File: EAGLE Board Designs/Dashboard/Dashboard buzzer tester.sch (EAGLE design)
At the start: 0 parts

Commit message: Buzzer test circuit additions
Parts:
- added C21: CAPACITOR_0603_10V_0.1UF, HyTechDevices:CAPACITOR_0603_10V_0.1UF
- added K1: CPC1002N, HyTechDevices - Copy:CPC1002N
- added Q7: TRANSISTOR_P_MOS_SOT23_SI2369DS-T1-GE3, HyTechDevices:TRANSISTOR_P_MOS_SOT23_SI2369DS-T1-GE3
- added R16: RESISTOR_0603_150K, HyTechDevices:RESISTOR_0603_150K
- added R17: RESISTOR_0603_2K, HyTechDevices:RESISTOR_0603_2K
- added R18: RESISTOR_0603_1K, HyTechDevices:RESISTOR_0603_1K
- added R19: RESISTOR_0603_620, HyTechDevices:RESISTOR_0603_620
- added R22: RESISTOR_0603_3.9K, HyTechDevices:RESISTOR_0603_3.9K
- added U$1: BUZZER_3_PIN_CPT-3011C-120, HyTechDevices:BUZZER_3_PIN_CPT-3011C-120
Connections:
- new net +12V: K1.DC+
- new net BUZZER_CTRL: K1.CONTROL+
- new net BUZZER_OUT: C21.1, K1.DC-, R17.1
- new net GND: C21.2, Q7.S, R17.2, R18.1, U$1.GND
- new net N$20: R16.2, R22.1, U$1.F
- new net N$22: Q7.G, R22.2
- new net N$29: R16.1, R19.1
- new net N$41: Q7.D, R19.2, U$1.VDD
- new net N$68: K1.CONTROL-, R18.2
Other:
- note added: "PCB for testing piezo buzzer for dashboard"
- note added: "Youssef Jaafar"

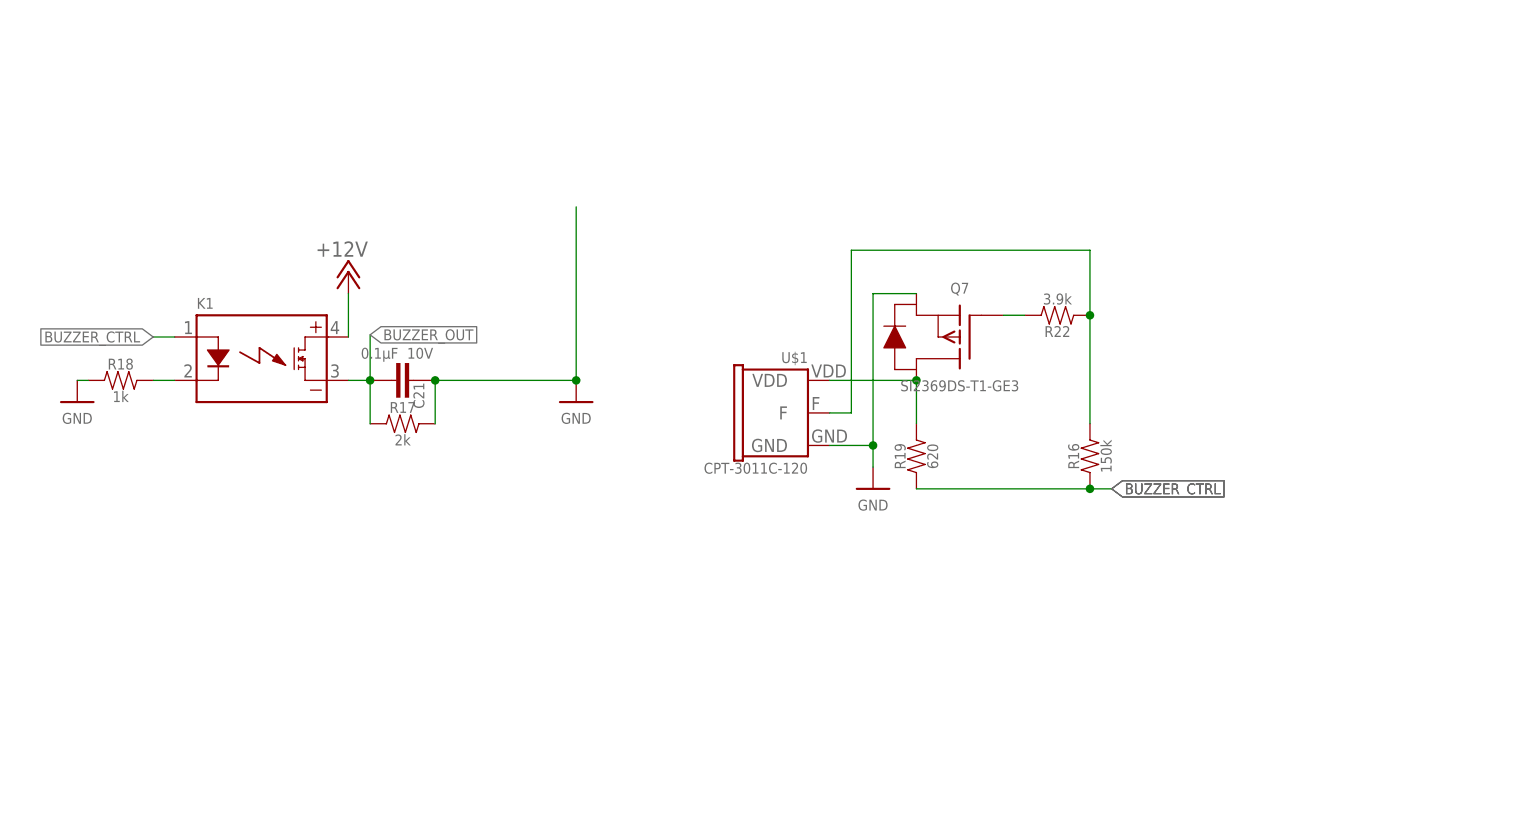
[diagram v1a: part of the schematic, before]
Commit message: Buzzer tester schematic and board started
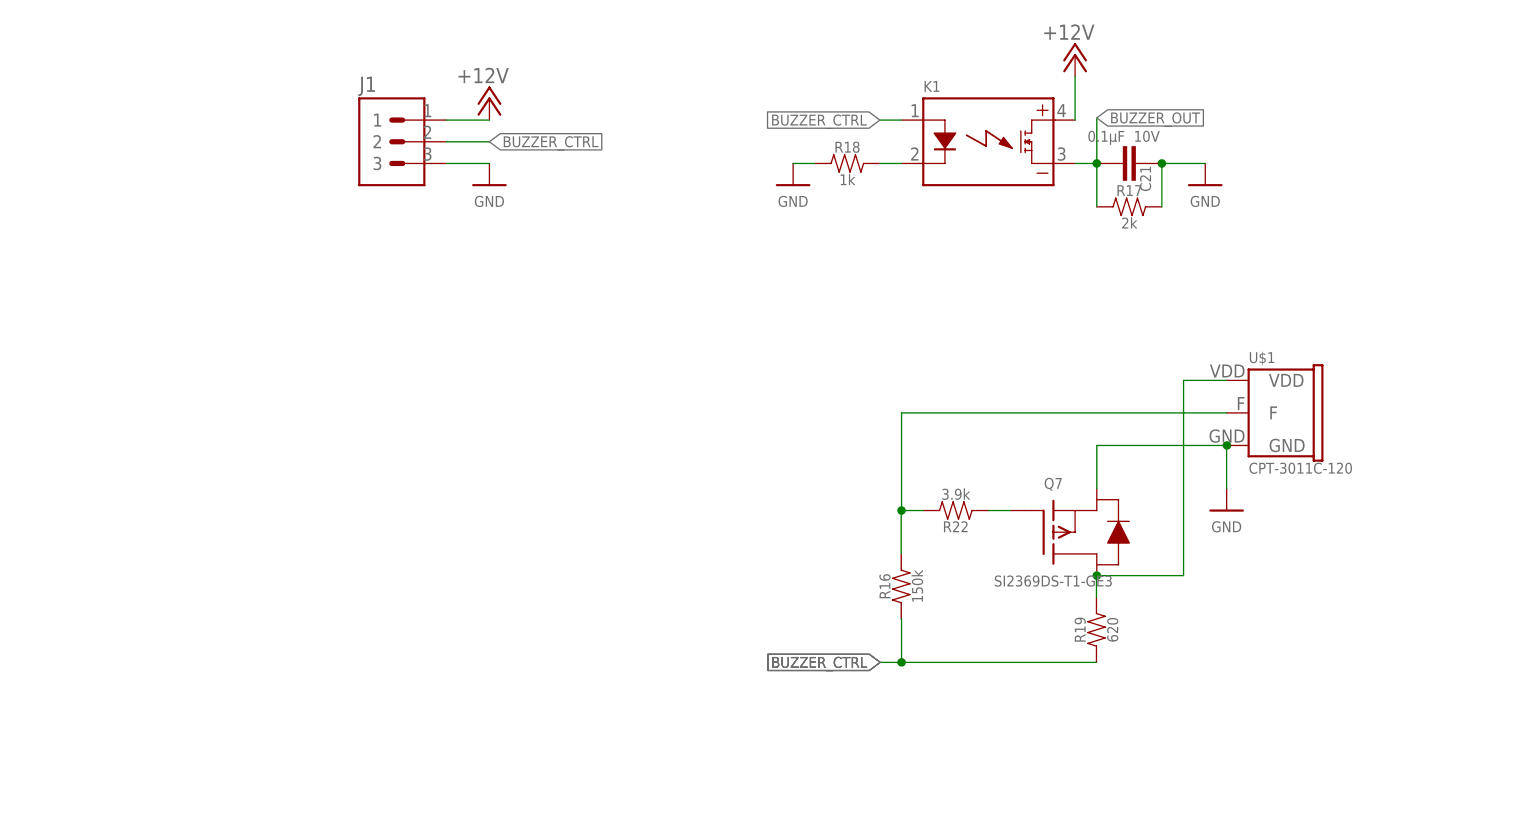
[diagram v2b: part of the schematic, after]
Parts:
- added J1: (no value), HyTechDevices - Copy:CONNECTOR-3
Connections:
- removed net N$20: R16.2, R22.1, U$1.F
- removed net N$22: Q7.G, R22.2
- new net N$3: Q7.G, R22.1
- new net N$4: R16.2, R22.2, U$1.F
- net +12V: now also J1.1
- net BUZZER_CTRL: now also J1.2
- net GND: now also J1.3
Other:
- moved on the sheet: C21, K1, Q7, R16, R17, R18, R19, R22, U$1

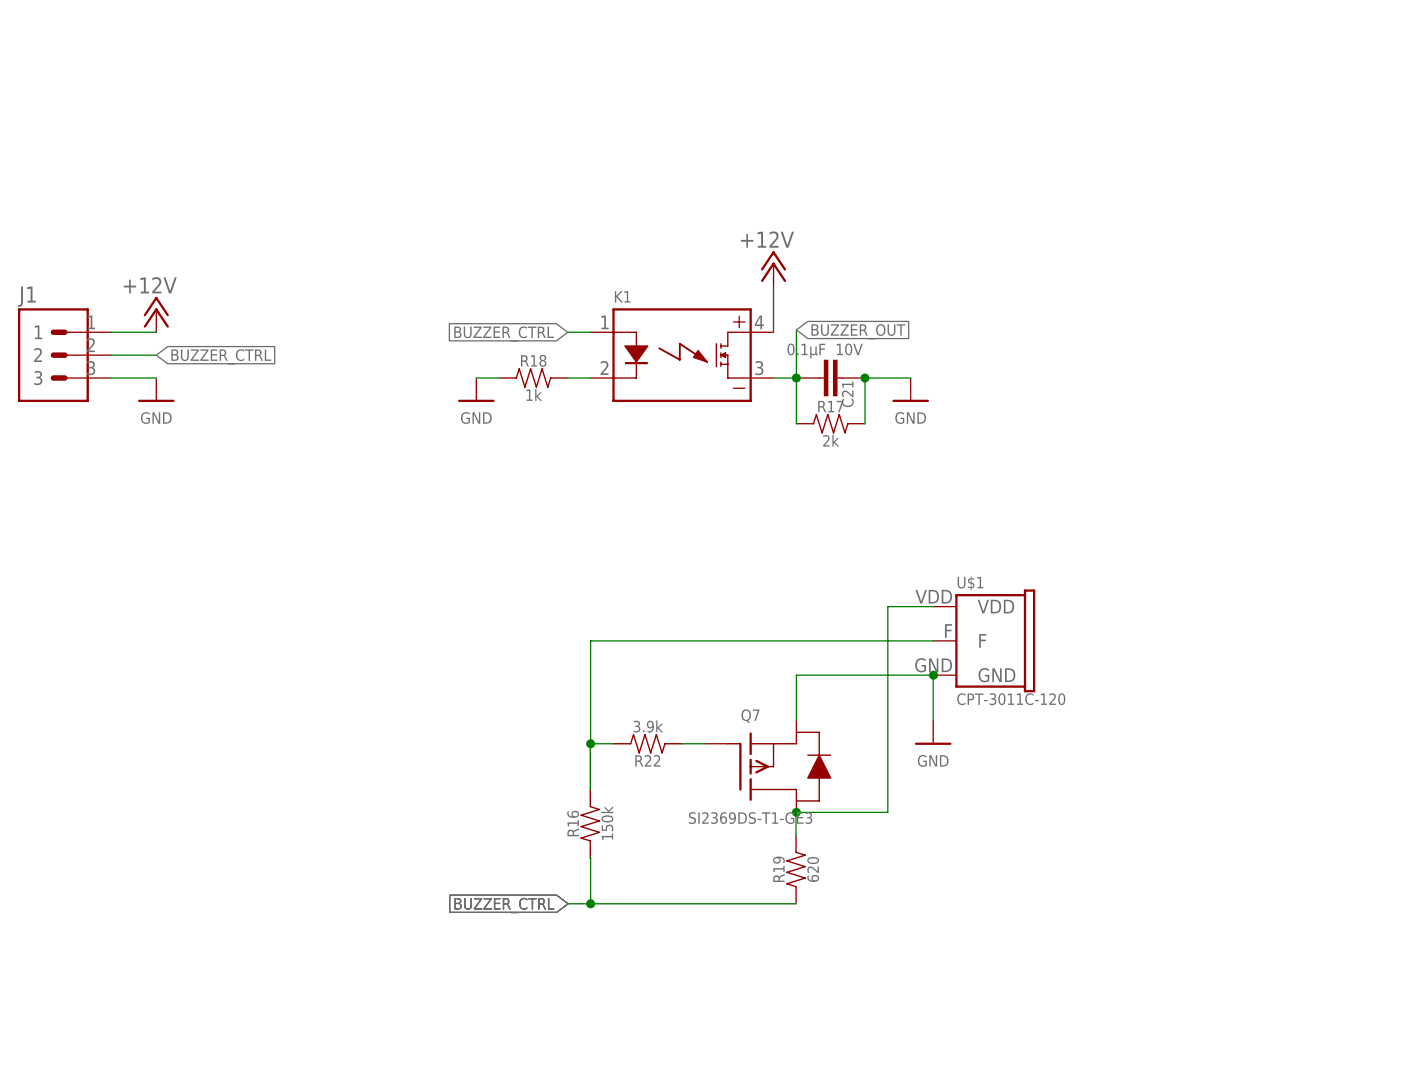
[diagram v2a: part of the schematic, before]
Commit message: Buzzer tester board design finished
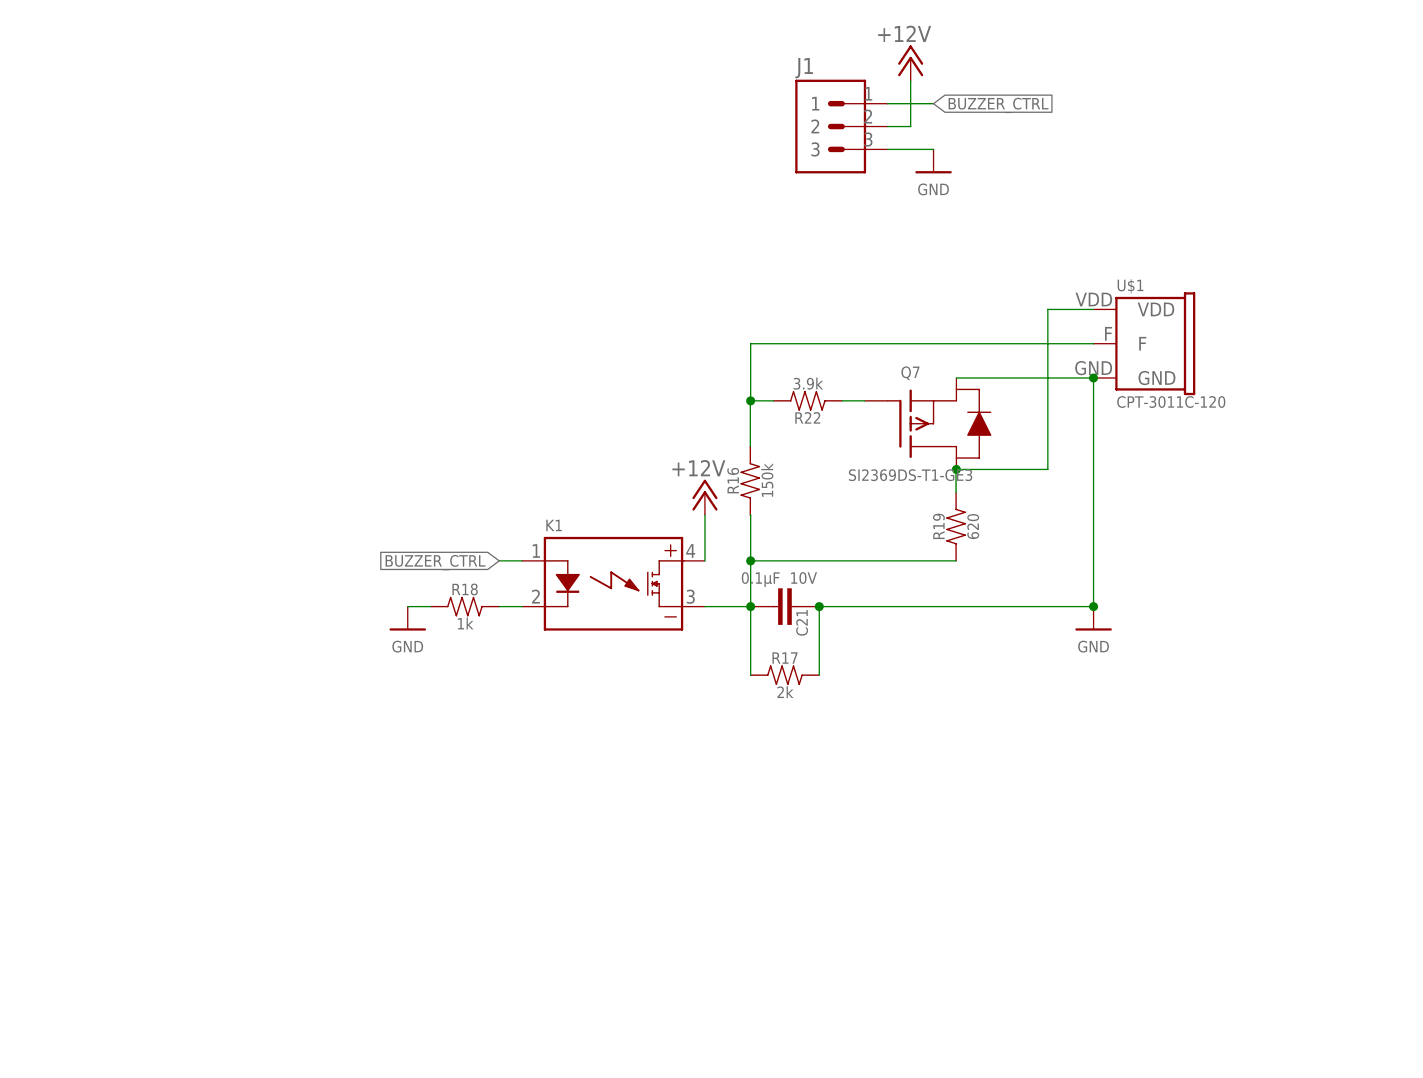
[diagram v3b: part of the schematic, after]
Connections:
- removed net N$1: R16.1, R19.1
- net +12V: now also J1.2; no longer J1.1
- net BUZZER_CTRL: now also J1.1; no longer J1.2
- net BUZZER_OUT: now also R16.1, R19.1
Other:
- moved on the sheet: C21, J1, K1, Q7, R16, R17, R18, R19, R22, U$1
